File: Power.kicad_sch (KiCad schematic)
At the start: 0 parts

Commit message: [200~⬜⬜⬜⬜⬜⬜⬜⬜⬜⬜⬜⬜🟥🟥🟥🟥🟥🟥🟥🟥🟥🟥⬜⬜⬜⬜⬜⬜
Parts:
- added C1, C2: 1uF, symbol Device:C
- added IC5: LM5085MY_NOPB, ExternalFootprints:SOP65P490X109-9N, symbol LM5085MY_NOPB:LM5085MY_NOPB
- added IC6: CYPD3177-24LQXQ, ExternalFootprints:QFN50P400X400X60-25N-D, symbol CYPD3177-24LQXQ:CYPD3177-24LQXQ
- added J1: USB_C_Receptacle_PowerOnly_6P, symbol Connector:USB_C_Receptacle_PowerOnly_6P
- added TP1: USBPowerFault, symbol Connector:TestPoint
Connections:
- new net: IC6.9 (FAULT), TP1.1
- new net: IC6.14 (CC2), J1.B5 (CC2)
- new net: IC6.15 (CC1), J1.A5 (CC1)
- new net: IC6.18 (VBUS_IN), J1.A9 (VBUS), J1.B9 (VBUS)
- new net: C2.2, IC6.23 (VDDD)
- new net: C1.2, IC6.24 (VCCD)
- new net GND: C1.1, C2.1, IC6.19 (GND_1), IC6.22 (GND_2), IC6.25 (GND_3), J1.A12 (GND), J1.B12 (GND)
- no-connect marks 0 -> 5

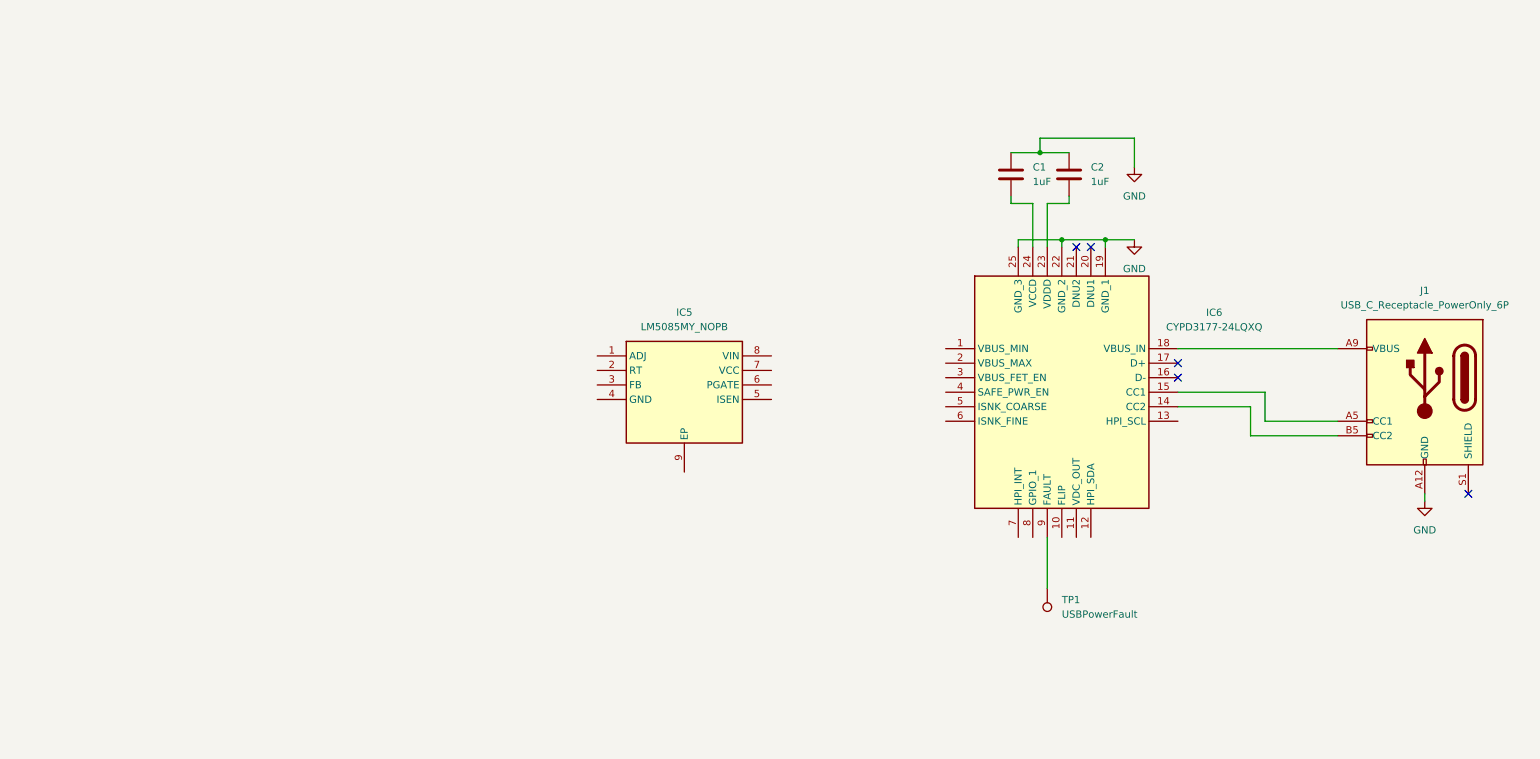
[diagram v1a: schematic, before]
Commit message: Added initial USBC Power
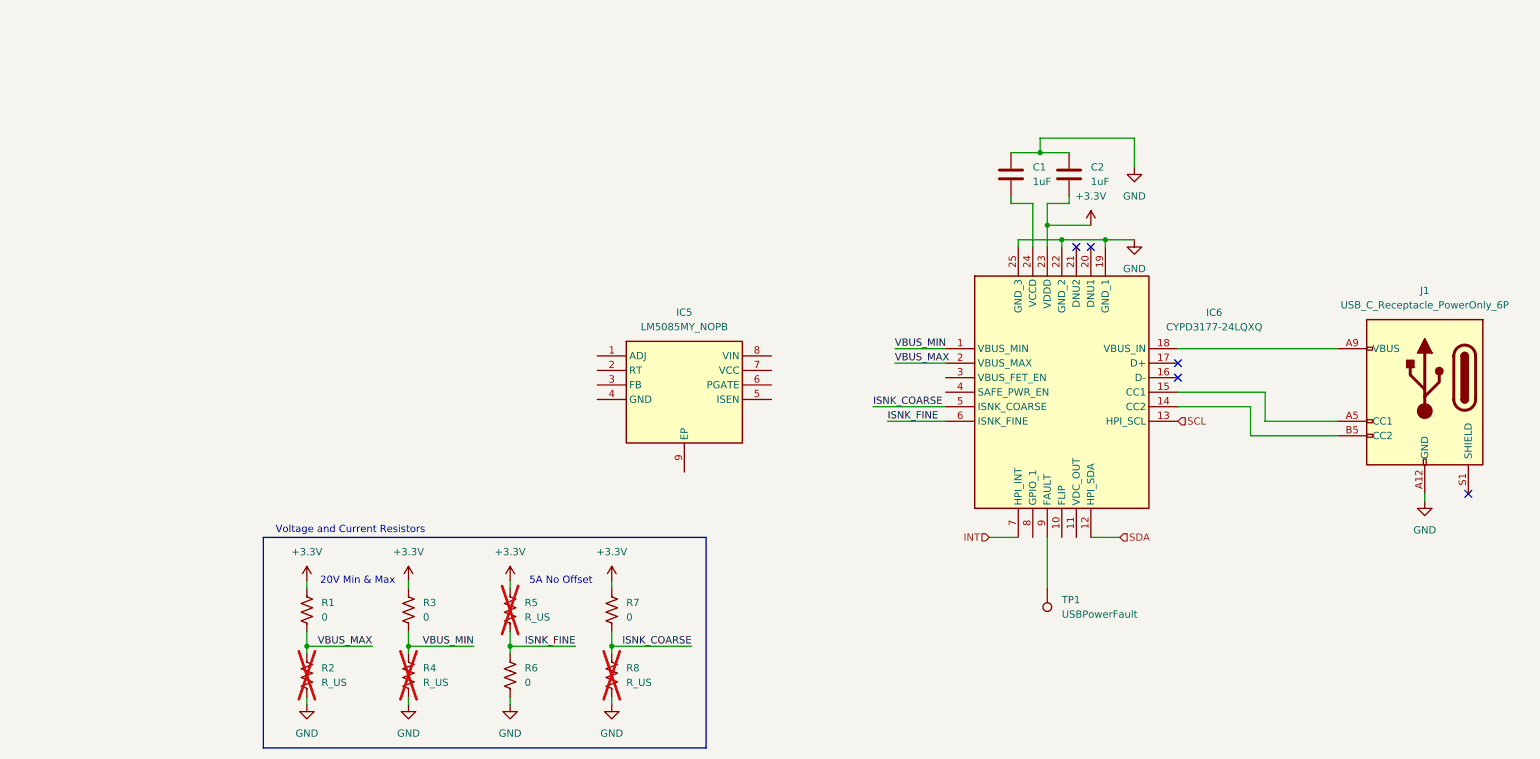
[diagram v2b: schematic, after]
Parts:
- added R1, R3, R6, R7: 0, symbol Device:R_US
- added R2, R4, R5, R8: R_US, symbol Device:R_US
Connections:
- net GND: now also C1.2, R2.2, R4.2, R6.2, R8.2; no longer C1.1
- net VBUS_MIN: now reaches IC6.1 (VBUS_MIN)
- net VBUS_MIN: now also R3.2, R4.1
- net SDA: now reaches IC6.12 (HPI_SDA)
- net SCL: now reaches IC6.13 (HPI_SCL)
- net VBUS_MAX: now reaches IC6.2 (VBUS_MAX)
- net VBUS_MAX: now also R1.2, R2.1
- net +3.3V: now reaches C2.2, IC6.23 (VDDD)
- net +3.3V: now also R1.1, R3.1, R5.1, R7.1
- net at IC6.24 (VCCD): now also C1.1; no longer C1.2
- net ISNK_COARSE: now reaches IC6.5 (ISNK_COARSE)
- net ISNK_COARSE: now also R7.2, R8.1
- net ISNK_FINE: now reaches IC6.6 (ISNK_FINE)
- net ISNK_FINE: now also R5.2, R6.1
- net INT: now reaches IC6.7 (HPI_INT)
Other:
- note added: "20V Min & Max"
- note added: "5A No Offset"
- note added: "Voltage and Current Resistors"
- moved on the sheet: C1

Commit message: updated power stuff
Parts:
- removed IC5: LM5085MY_NOPB, ExternalFootprints:SOP65P490X109-9N, symbol LM5085MY_NOPB:LM5085MY_NOPB
- added C3, C4: 3.3uF, symbol Device:C
- added C5, C6: 1uF, Capacitor_SMD:C_0805_2012Metric, symbol Device:C_Small
- added Q1: IRF9358TRPBF, Package_SO:SO-8_3.9x4.9mm_P1.27mm, symbol Device:Q_Dual_PMOS_S1G1S2G2D2D2D1D1
- added Q2: BSL308PEH6327XTSA1, Package_TO_SOT_SMD:SOT-23-6, symbol Device:Q_Dual_PMOS_G1S2G2D2S1D1
- added R10, R12: 1k, Resistor_SMD:R_0805_2012Metric, symbol Device:R
- added R11, R9: 10k, Resistor_SMD:R_0805_2012Metric, symbol Device:R
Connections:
- net GND: now also C3.2, C4.2
- net FAULT: now reaches IC6.9 (FAULT), TP1.1
- net FLIP: now reaches IC6.10 (FLIP)
- net VDC_OUT: now reaches IC6.11 (VDC_OUT)
- net VBUS_IN: now reaches IC6.18 (VBUS_IN), J1.A9 (VBUS), J1.B9 (VBUS)
- net VBUS_IN: now also C3.1, C4.1, C5.1, Q1.5 (D), Q1.6 (D), Q2.4 (D), R11.1, R9.1
- net VBUS_FET_EN: now reaches IC6.3 (VBUS_FET_EN)
- net VBUS_FET_EN: now also R12.2
- net SAFE_PWR_EN: now reaches IC6.4 (SAFE_PWR_EN)
- new net: C5.2, C6.2, Q1.2 (G), Q1.4 (G), R11.2, R12.1
- new net: Q1.1 (S), Q1.3 (S)
- new net: Q2.2 (S), Q2.5 (S)
- new net: Q2.1 (G), Q2.3 (G), R10.1, R9.2
- new net SAFE_5V: Q2.6 (D)
- new net SAFE_5V_EN: R10.2
- new net VBUS_OUT: C6.1, Q1.7 (D), Q1.8 (D)
- no-connect marks 5 -> 6
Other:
- added sheet 20V to 5V Buck (buck.kicad_sch)
- note added: "20V->5V Buck"
- note added: "5V->3.3V LDO"
- note added: "Enable Mosfets"
- note added: "USB-C PD Controller"
- moved on the sheet: TP1

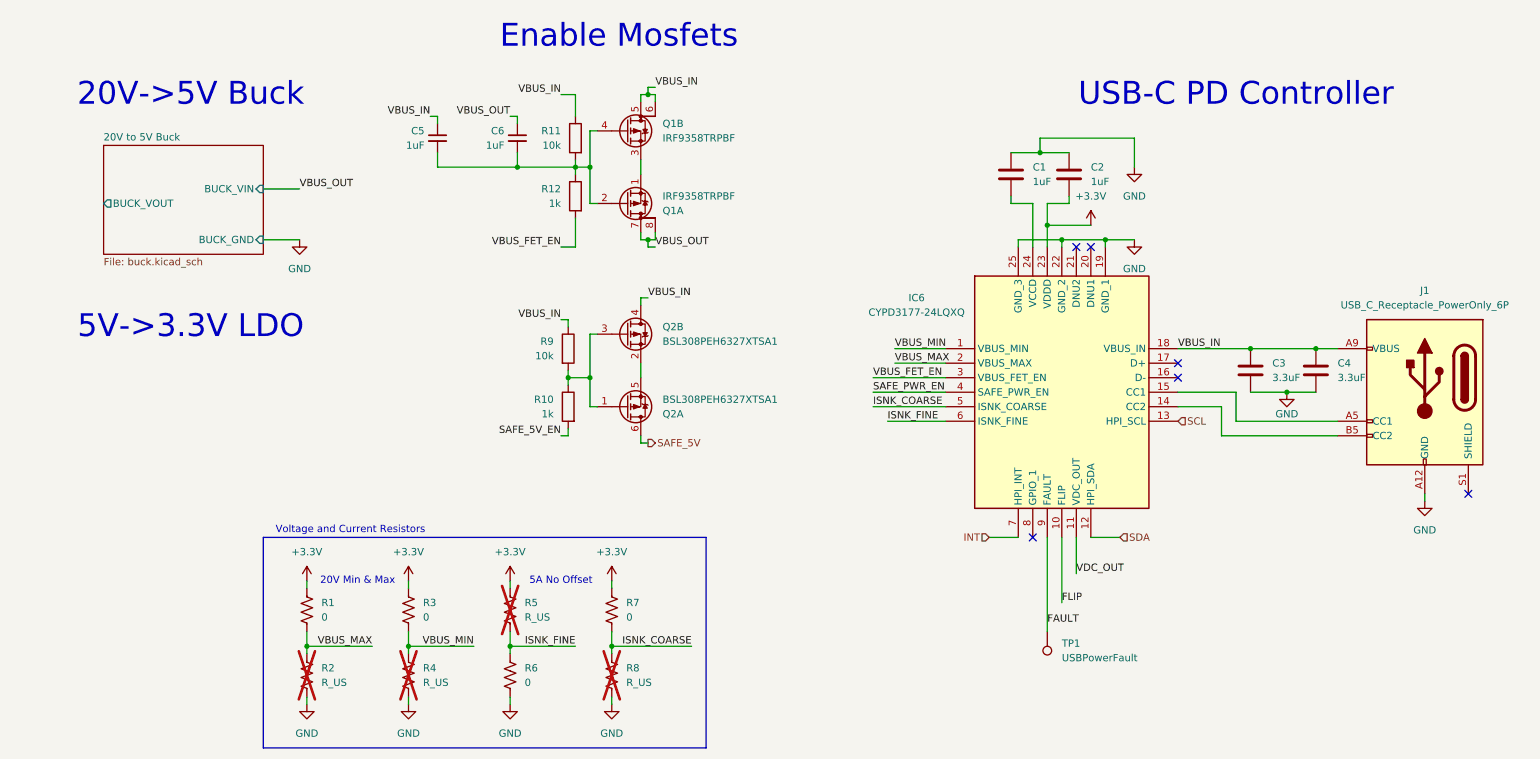
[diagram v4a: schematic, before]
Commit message: added LDO and fixed connections in power
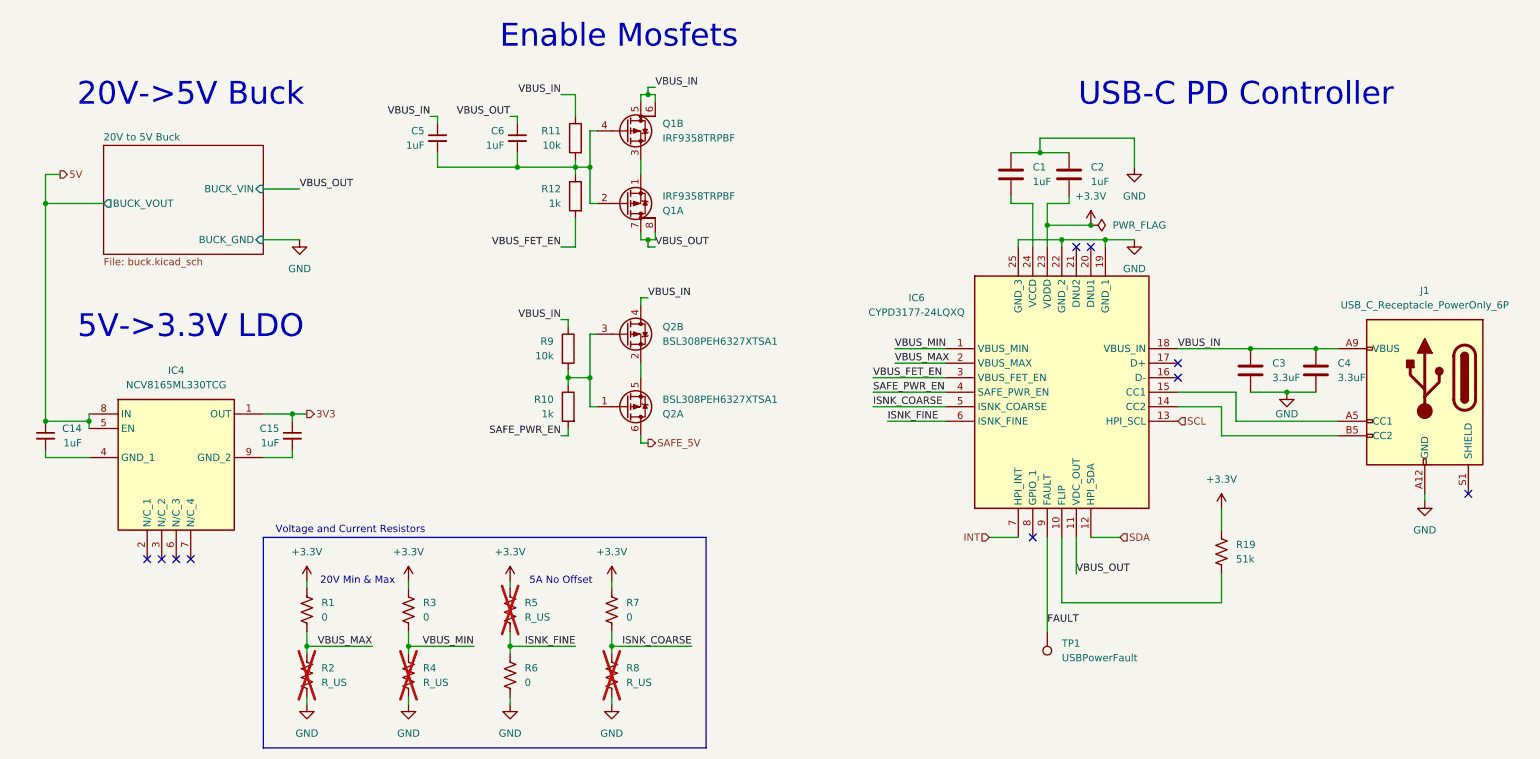
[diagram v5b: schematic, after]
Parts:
- added C14, C15: 1uF, Capacitor_SMD:C_0805_2012Metric, symbol Device:C_Small
- added IC4: NCV8165ML330TCG, SON65P300X300X100-9N-D, symbol NCV8165ML330TCG:NCV8165ML330TCG
- added R19: 51k, symbol Device:R_US
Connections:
- net SAFE_5V_EN is gone; now on net SAFE_PWR_EN: R10.2
- net VDC_OUT is gone; now on net VBUS_OUT: IC6.11 (VDC_OUT)
- net +3.3V: now also R19.1
- net FLIP: no longer names the net of IC6.10 (FLIP)
- net FLIP: now also R19.2
- new net: C14.2, IC4.4 (GND_1)
- new net: C15.2, IC4.9 (GND_2)
- new net 3V3: C15.1, IC4.1 (OUT)
- new net 5V: C14.1, IC4.5 (EN), IC4.8 (IN)
- no-connect marks 6 -> 10

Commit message: usb uart fixes and ldo
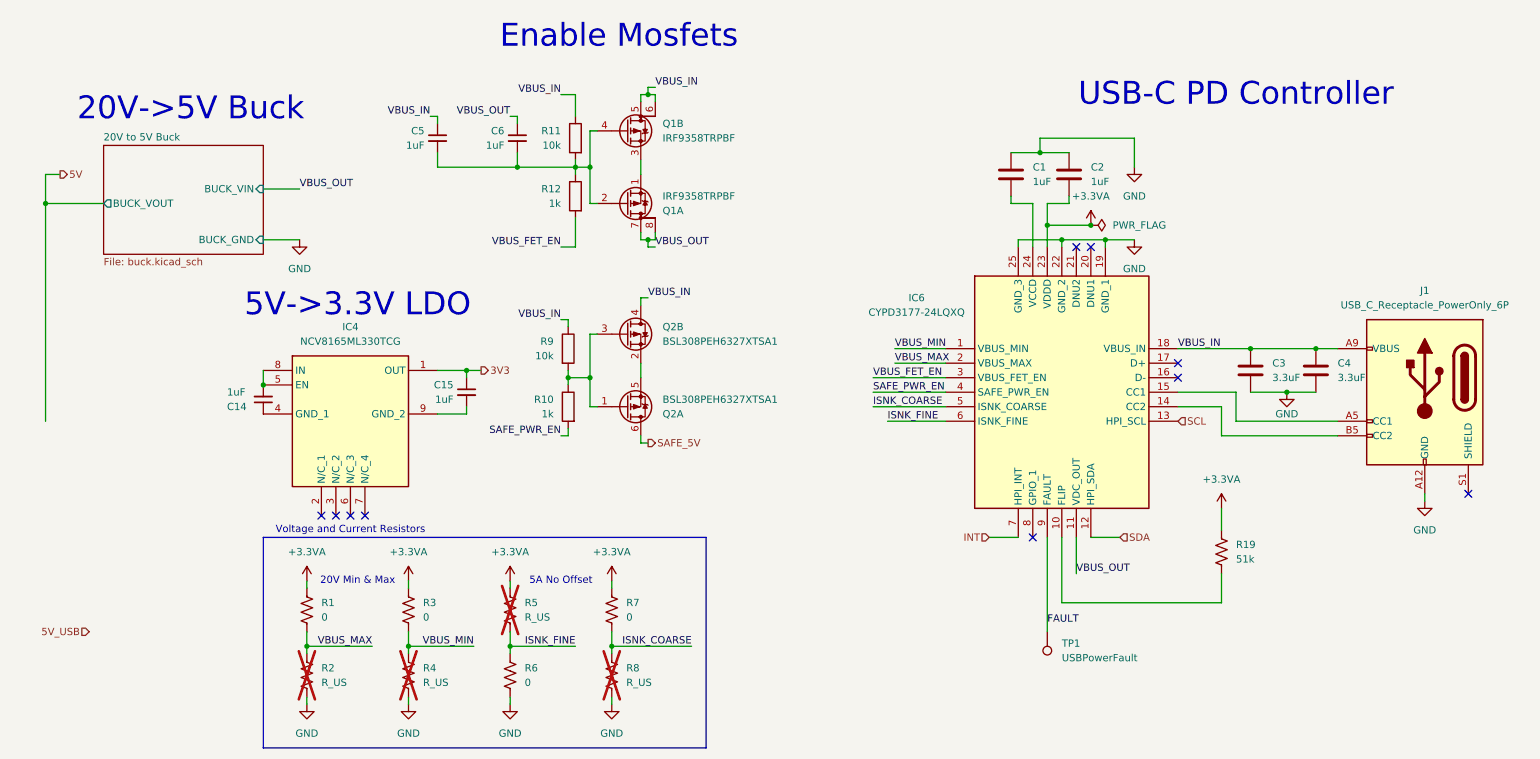
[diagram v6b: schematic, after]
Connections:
- net 5V: no longer C14.1, IC4.5 (EN), IC4.8 (IN)
- net at IC4.4 (GND_1): now also C14.1; no longer C14.2
- net +3.3V renamed +3.3VA
- new net: C14.2, IC4.5 (EN), IC4.8 (IN)
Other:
- moved on the sheet: C14, C15, IC4

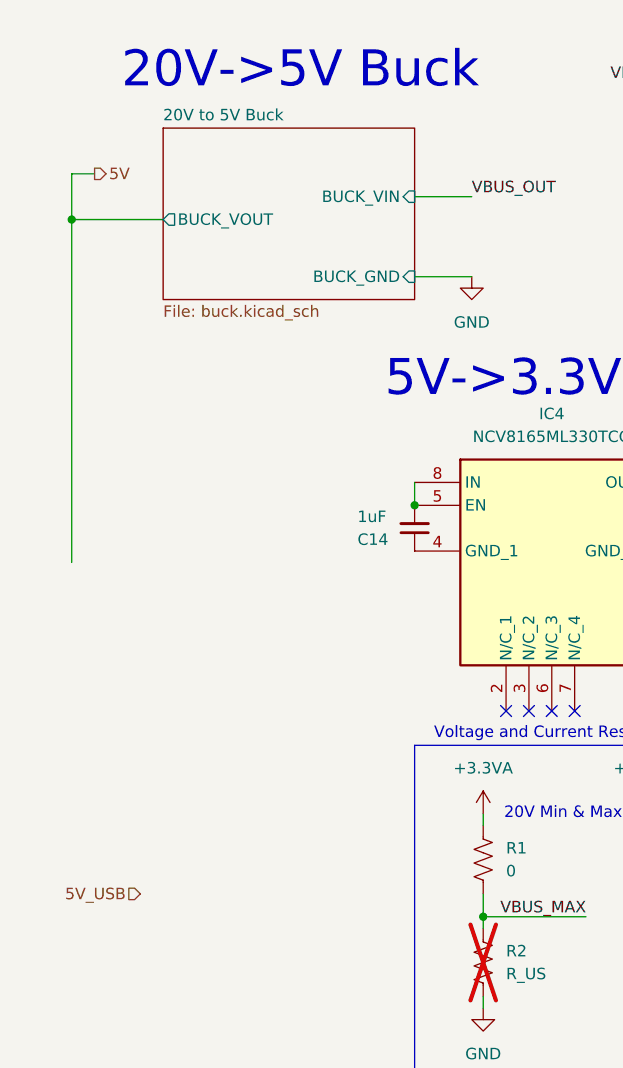
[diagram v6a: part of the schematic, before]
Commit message: me when the power is muxing and pinning esp32
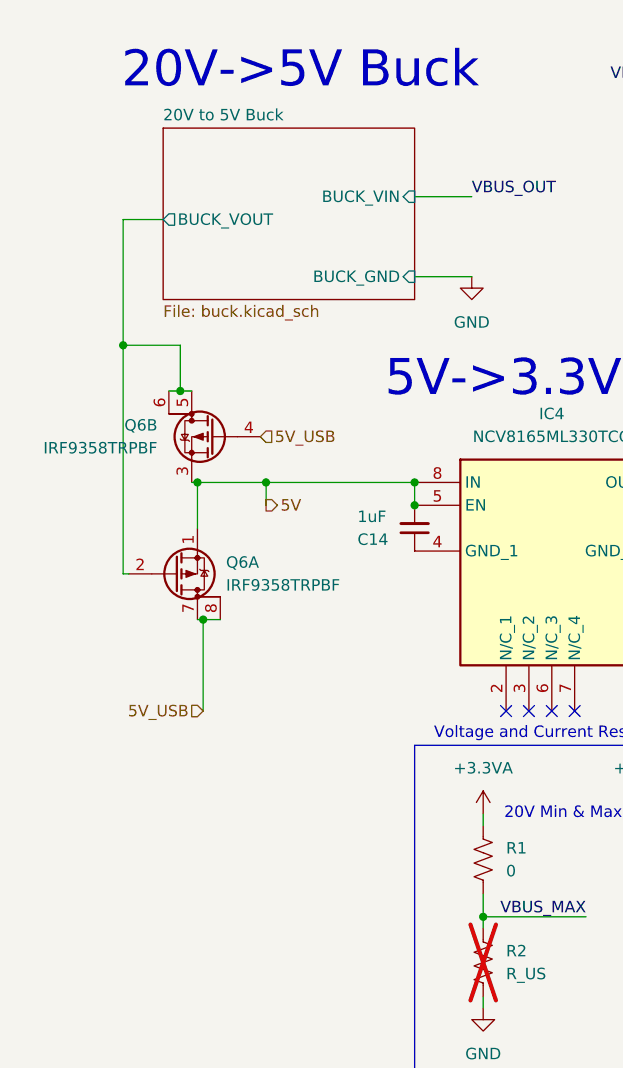
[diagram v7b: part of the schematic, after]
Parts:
- added Q6: IRF9358TRPBF, Package_SO:SO-8_3.9x4.9mm_P1.27mm, symbol Device:Q_Dual_PMOS_S1G1S2G2D2D2D1D1
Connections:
- net 5V: now also C14.2, IC4.5 (EN), IC4.8 (IN), Q6.1 (S), Q6.3 (S)
- net 5V_USB: now also Q6.4 (G), Q6.7 (D), Q6.8 (D)
- new net 20V to 5V Buck/BUCK_VOUT: Q6.2 (G), Q6.5 (D), Q6.6 (D)
